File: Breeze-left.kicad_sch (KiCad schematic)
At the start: 72 parts, among them SW1 CHOCXHSPCB-1U, SW10 CHOCXHSPCB-1U, SW11 CHOCXHSPCB-1U, SW12 CHOCXHSPCB-1U, SW13 CHOCXHSPCB-1U, SW14 CHOCXHSPCB-1U, SW15 CHOCXHSPCB-1U, SW16 CHOCXHSPCB-1U, SW17 CHOCXHSPCB-1U, SW18 CHOCXHSPCB-1U, SW19 CHOCXHSPCB-1U, SW2 CHOCXHSPCB-1U, SW20 CHOCXHSPCB-1U, SW21 CHOCXHSPCB-1U, SW22 CHOCXHSPCB-1U, SW23 CHOCXHSPCB-1U, SW24 CHOCXHSPCB-1U, SW3 CHOCXHSPCB-1U, SW4 CHOCXHSPCB-1U, SW5 CHOCXHSPCB-1U, SW6 CHOCXHSPCB-1U, SW7 CHOCXHSPCB-1U, SW8 CHOCXHSPCB-1U, SW9 CHOCXHSPCB-1U

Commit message: do left
use gitignore
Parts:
- removed BATT_CONN1: ~, Breeze:BATT_PADS, symbol Breeze:BATT_PADS
- removed H18, H19, H2, H3, H4, H5, H6, H7, H8, H9: M3-HOLE, Breeze:M3-HOLE, symbol Breeze-rescue:3M-HOLE-Merkaba_Rev0-rescue-Breeze-rescue
- added H1, H10, H2, H3, H4, H5, H6, H7, H8, H9: MountingHole_M3, MountingHole:MountingHole_3.2mm_M3_ISO7380_Pad, symbol Mechanical:MountingHole_Pad
- added J1: Conn_01x02, Breeze:BATT_PADS, symbol Connector_Generic:Conn_01x02
- D1, D10, D11, D12, D13, D14, D15, D16, D17, D18, D19, D2, D20, D21, D22, D23, D24, D3, D4, D5, D6, D7, D8, D9: value DIODE -> 1N4007W; footprint Breeze:SOD-123FL -> Breeze:SOD-123FL_L2.7-W1.8-LS3.7-RD; symbol Breeze-rescue:Diode-cache-Merkaba_Rev0-rescue-Breeze-rescue -> Diode:1N4007
- D25: renamed from DTC1; value DIODE -> 1N4007W; footprint Breeze:SOD-123FL -> Breeze:SOD-123FL_L2.7-W1.8-LS3.7-RD; symbol Breeze-rescue:Diode-cache-Merkaba_Rev0-rescue-Breeze-rescue -> Diode:1N4007
- D26: renamed from DTC2; value DIODE -> 1N4007W; footprint Breeze:SOD-123FL -> Breeze:SOD-123FL_L2.7-W1.8-LS3.7-RD; symbol Breeze-rescue:Diode-cache-Merkaba_Rev0-rescue-Breeze-rescue -> Diode:1N4007
- D27: renamed from DTC3; value DIODE -> 1N4007W; footprint Breeze:SOD-123FL -> Breeze:SOD-123FL_L2.7-W1.8-LS3.7-RD; symbol Breeze-rescue:Diode-cache-Merkaba_Rev0-rescue-Breeze-rescue -> Diode:1N4007
- D28: renamed from DTC4; value DIODE -> 1N4007W; footprint Breeze:SOD-123FL -> Breeze:SOD-123FL_L2.7-W1.8-LS3.7-RD; symbol Breeze-rescue:Diode-cache-Merkaba_Rev0-rescue-Breeze-rescue -> Diode:1N4007
- renumbered LGO1 to G1, STABL1 to H11, PWR1 to SW1, RST1 to SW2, MCU-MAIN1 to U1, SW1 to XS1, SW10 to XS10, SW11 to XS11, SW12 to XS12, SW13 to XS13, SW14 to XS14, SW15 to XS15, SW16 to XS16, SW17 to XS17, SW18 to XS18, SW19 to XS19, SW2 to XS2, SW20 to XS20, SW21 to XS21, SW22 to XS22, SW23 to XS23, SW24 to XS24, TC1 to XS25, TC2 to XS26, TC3 to XS27, TC4 to XS28, SW3 to XS3, SW4 to XS4, SW5 to XS5, SW6 to XS6, SW7 to XS7, SW8 to XS8, SW9 to XS9
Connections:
- net GND: now also H1.1, H10.1, H2.1, H3.1, H4.1, H5.1, H6.1, H7.1, H8.1, H9.1, J1.1 (Pin_1)
- net at SW1.2 (B): now also J1.2 (Pin_2)
- net BAT_PLUS renamed +BATT
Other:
- moved on the sheet: D1, D10, D11, D12, D13, D14, D15, D16, D17, D18, D19, D2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

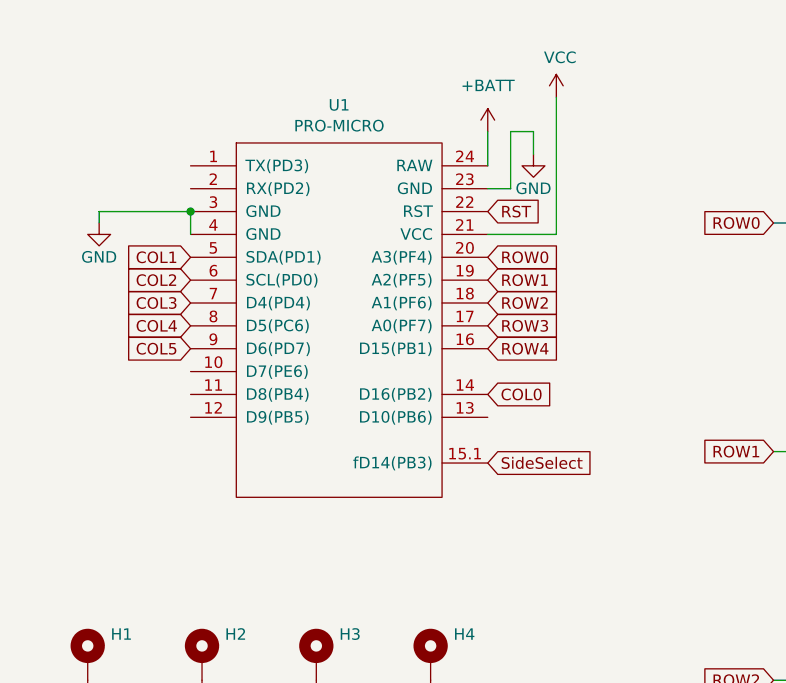
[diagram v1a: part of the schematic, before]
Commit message: redo left PCB, redraw supermini symbol
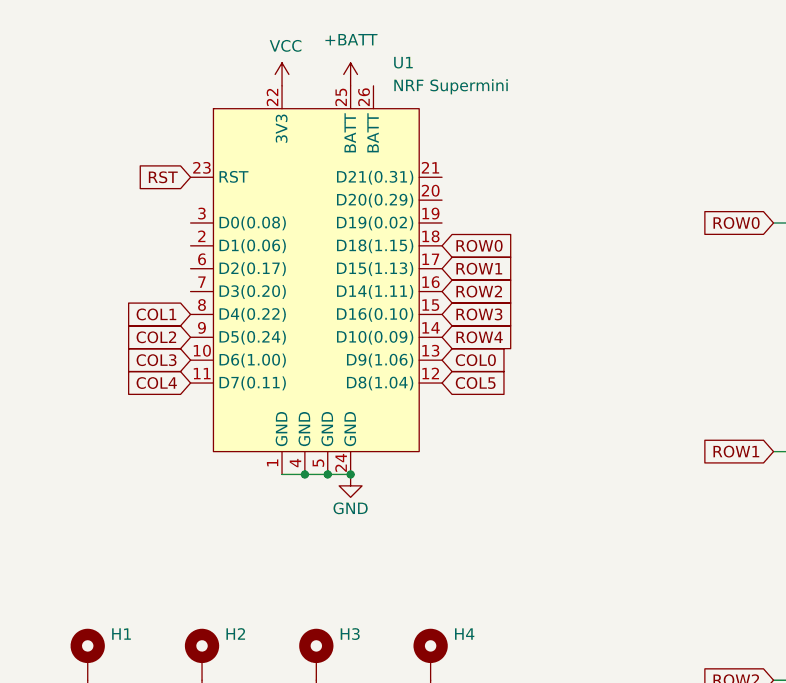
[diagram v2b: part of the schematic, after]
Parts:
- removed U1: PRO-MICRO, Breeze:ProMicro_1-Sided, symbol Breeze-rescue:ProMicro-Merkaba_Rev0-rescue-Breeze-rescue
- added U1: NRF Supermini, Breeze:NRF_Supermini, symbol Breeze:Pro_Micro
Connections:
- net +BATT: now also U1.25 (BATT)
- net COL0: now also U1.13 (D9(1.06))
- net COL1: now also U1.8 (D4(0.22))
- net COL2: now also U1.9 (D5(0.24))
- net COL3: now also U1.10 (D6(1.00))
- net COL4: now also U1.11 (D7(0.11))
- net COL5: now also U1.12 (D8(1.04))
- net GND: now also U1.1 (GND), U1.24 (GND), U1.4 (GND), U1.5 (GND)
- net ROW0: now also U1.18 (D18(1.15))
- net ROW1: now also U1.17 (D15(1.13))
- net ROW2: now also U1.16 (D14(1.11))
- net ROW3: now also U1.15 (D16(0.10))
- net ROW4: now also U1.14 (D10(0.09))
- net RST: now also U1.23 (RST)
- net VCC: now also U1.22 (3V3)

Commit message: done
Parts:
- XS1, XS10, XS11, XS12, XS13, XS14, XS15, XS16, XS17, XS18, XS19, XS2, XS20, XS21, XS22, XS23, XS24, XS25, XS26, XS27, XS28, XS3, XS4, XS5, XS6, XS7, XS8, XS9: symbol Breeze-rescue:CHOCXHSPCB-1U-cache-Merkaba_Rev0-rescue-Breeze-rescue -> Switch:SW_Push
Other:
- moved on the sheet: XS1, XS10, XS11, XS12, XS13, XS14, XS15, XS16, XS17, XS18, XS19, XS2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
